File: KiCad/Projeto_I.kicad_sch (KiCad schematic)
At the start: 42 parts, among them J1 PORTA, J2 PORTB, J3 PORTC, J4 USB_B_Micro, J5 Barrel_Jack_Switch, Q1 PMOS, SW1 reset, U1 PIC18F4550-IP, U2 LM7805, U3 LM358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

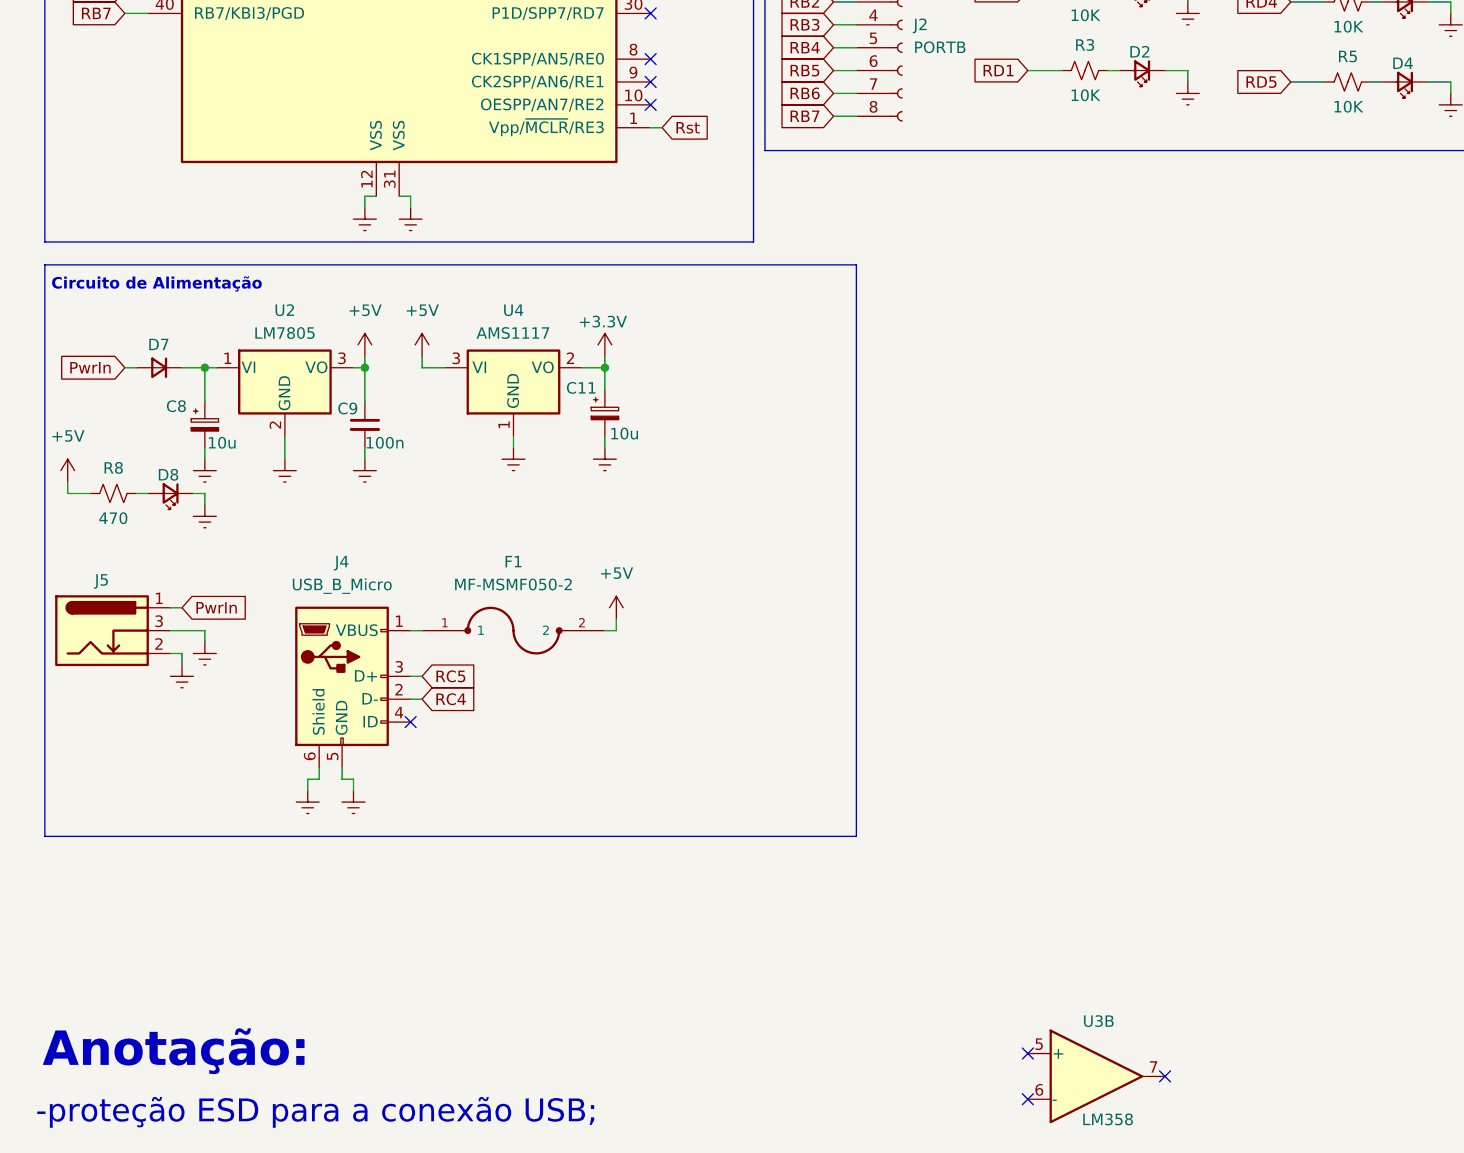
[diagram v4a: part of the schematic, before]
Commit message: Inclusão do circuito de proteção ESD para o USB
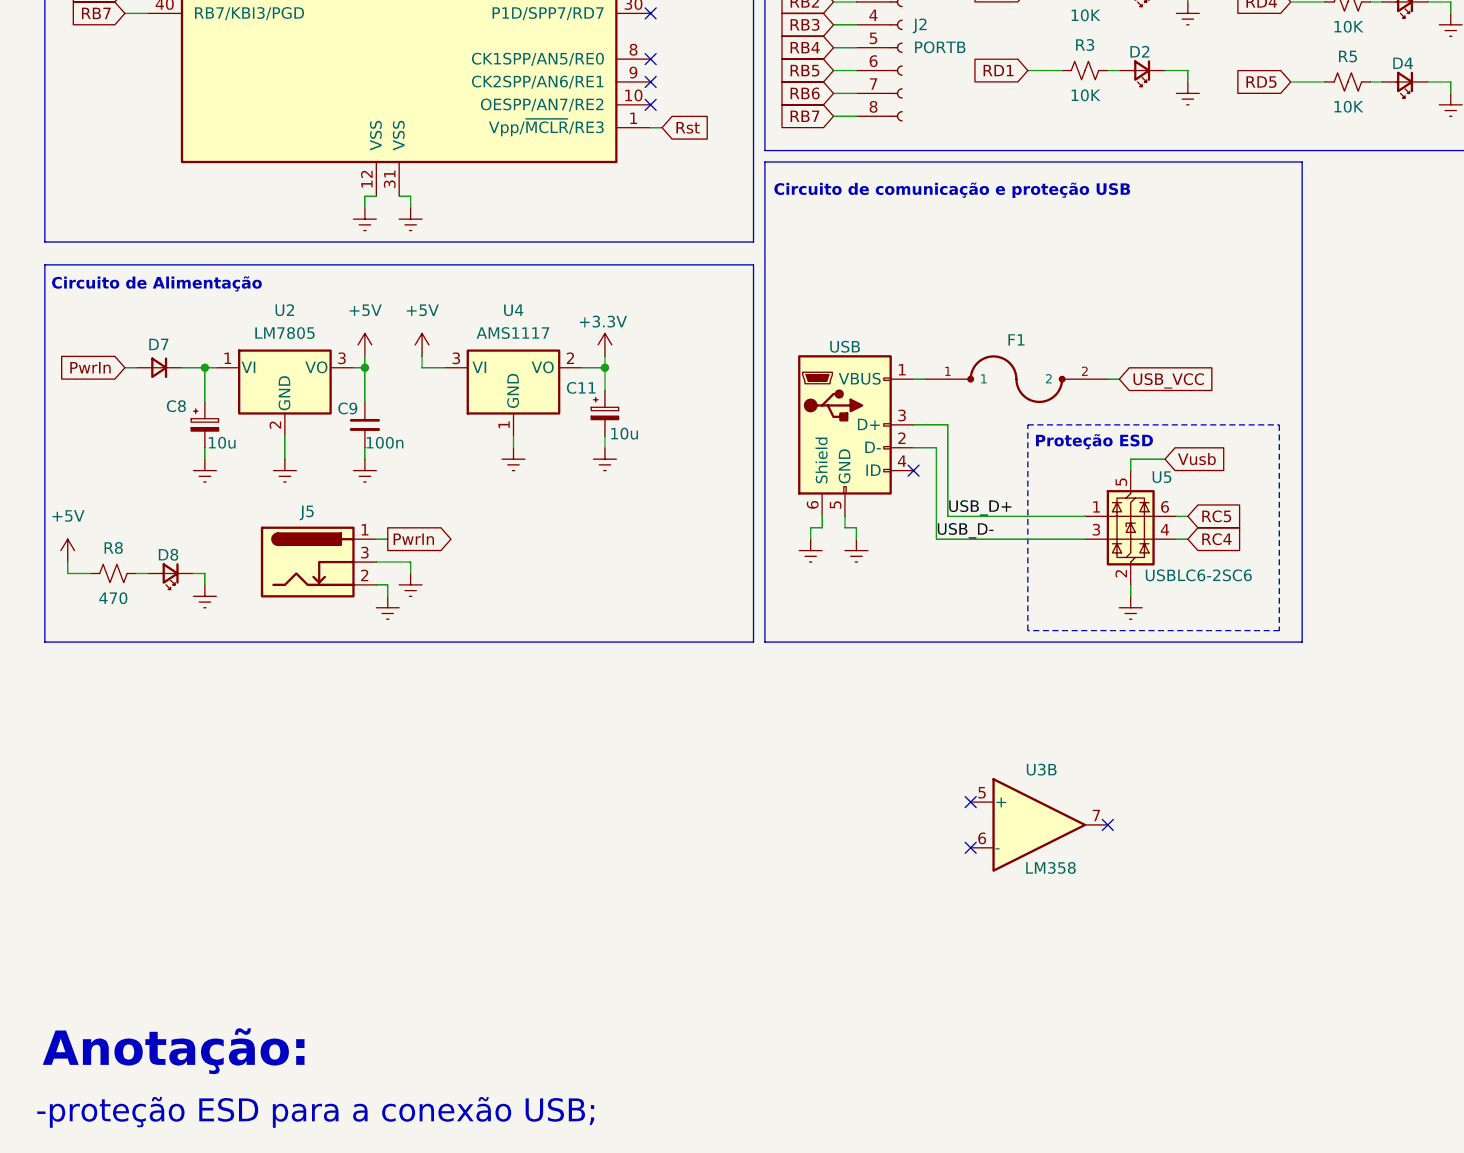
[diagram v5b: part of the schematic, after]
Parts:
- added U5: USBLC6-2SC6, Package_TO_SOT_SMD:SOT-23-6, symbol Power_Protection:USBLC6-2SC6
- J4: value USB_B_Micro -> USB
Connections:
- net +5V: no longer F1.2
- net Earth: now also U5.2 (GND)
- net RC4: now also U5.4 (I/O2); no longer J4.2 (D-)
- net RC5: now also U5.6 (I/O1); no longer J4.3 (D+)
- net USB_VCC: now also F1.2
- net Vusb: now also U5.5 (VBUS)
- new net USB_D+: J4.3 (D+), U5.1 (I/O1)
- new net USB_D-: J4.2 (D-), U5.3 (I/O2)
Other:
- note added: "Circuito de comunicação e proteção USB"
- note added: "Proteção ESD"
- moved on the sheet: D8, F1, J5, R8, U3B

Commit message: Atualização da PCB
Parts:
- removed U2: LM7805, Package_TO_SOT_THT:TO-220-3_Vertical, symbol Regulator_Linear:LM7805_TO220
- added U6: AMS1117-5.0, Package_TO_SOT_SMD:SOT-223-3_TabPin2, symbol Regulator_Linear:AMS1117-5.0
- C1, C2: footprint Capacitor_THT:C_Rect_L7.0mm_W2.5mm_P5.00mm -> Capacitor_THT:C_Disc_D5.0mm_W2.5mm_P2.50mm
- C11, C8: footprint Capacitor_THT:CP_Radial_D10.0mm_P3.80mm -> Capacitor_THT:CP_Radial_D5.0mm_P2.50mm
- Q1: footprint Package_TO_SOT_THT:TO-92L_HandSolder -> Package_TO_SOT_SMD:SOT-23
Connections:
- net +5V: now also U6.2 (VO)
- net Earth: now also U6.1 (GND)
- net at C8.1, D7.1 (K): now also U6.3 (VI)
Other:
- moved on the sheet: D8, J5, R8

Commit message: Atualização PCB
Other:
- note removed: "-proteção ESD para a conexão USB;"
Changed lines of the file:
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@@
-		)
-	)
-	(text "-proteção ESD para a conexão USB;"
-		(exclude_from_sim no)
-		(at 12.954 194.564 0)
-		(effects
-			(font
-				(size 2.54 2.54)
-				(thickness 0.3175)
-			)
-			(justify left)
 		)
 	)
@@
 	(label "USB_D-"
 		(at 113.03 130.81 0)
+		(fields_autoplaced yes)
 		(effects
 			(font
@@
 	(label "USB_D+"
 		(at 114.3 128.27 0)
+		(fields_autoplaced yes)
 		(effects
 			(font

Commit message: .
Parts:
- added J6: Alimentação, Connector_PinSocket_2.54mm:PinSocket_1x04_P2.54mm_Vertical, symbol Connector:Conn_01x04_Socket
- D2: value RD0 -> RD1
- D3: value RD0 -> RD4
- D4: value RD0 -> RD5
- D5: value RD0 -> RD2
- D6: value RD0 -> RD3
- Q1: value PMOS -> FDN340P
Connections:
- net +3.3V: now also J6.4 (Pin_4)
- net +5V: now also J6.3 (Pin_3)
- net Earth: now also J6.1 (Pin_1), J6.2 (Pin_2)
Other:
- note added: "-"
- note removed: "Falta definir o fet que será usado e o footprint dele."
- moved on the sheet: U3B
